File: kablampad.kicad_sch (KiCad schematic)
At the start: 25 parts, among them U1 RP2040_Zero

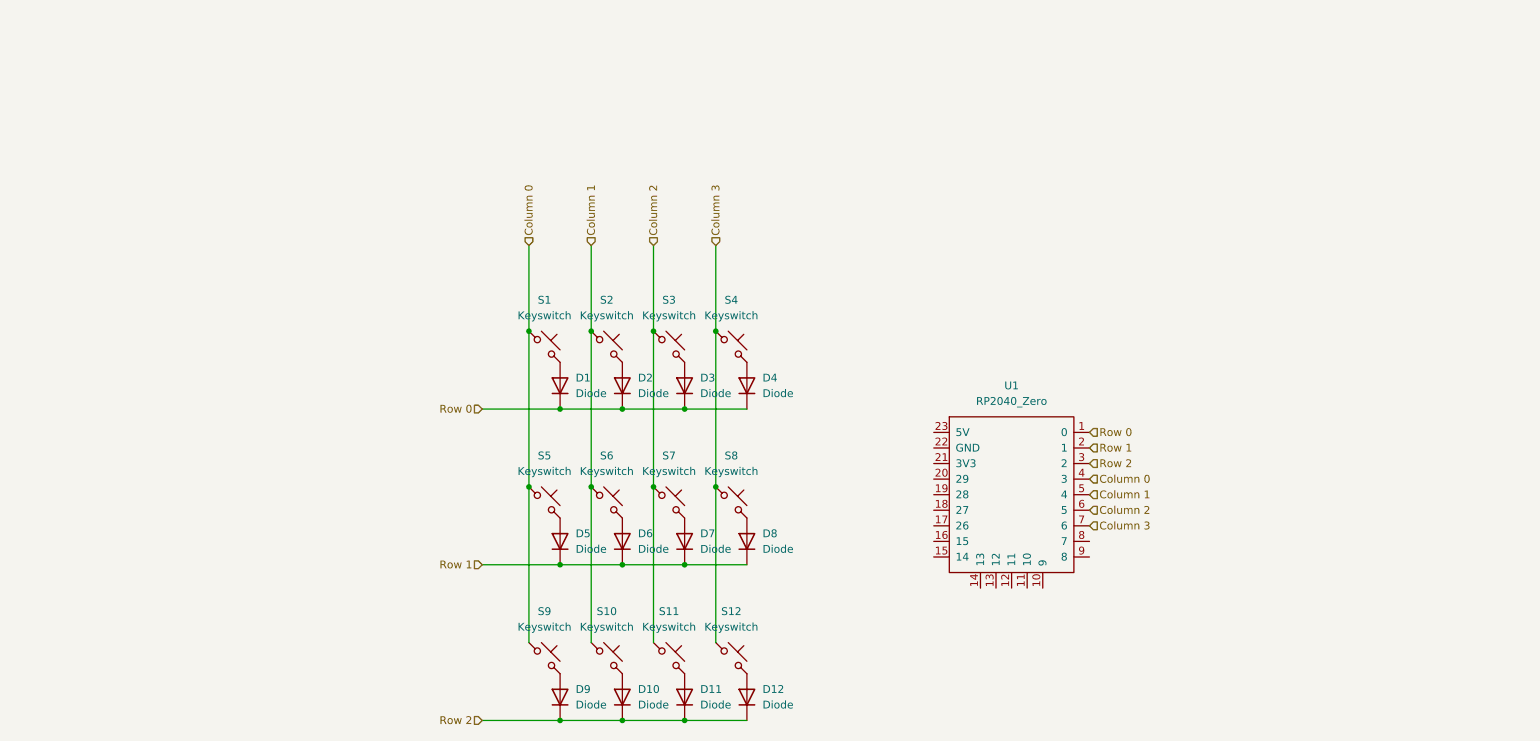
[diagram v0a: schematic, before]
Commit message: made kablamboard v1, idk how i'm gonna merge later (but that's a future problem, yaknow?)
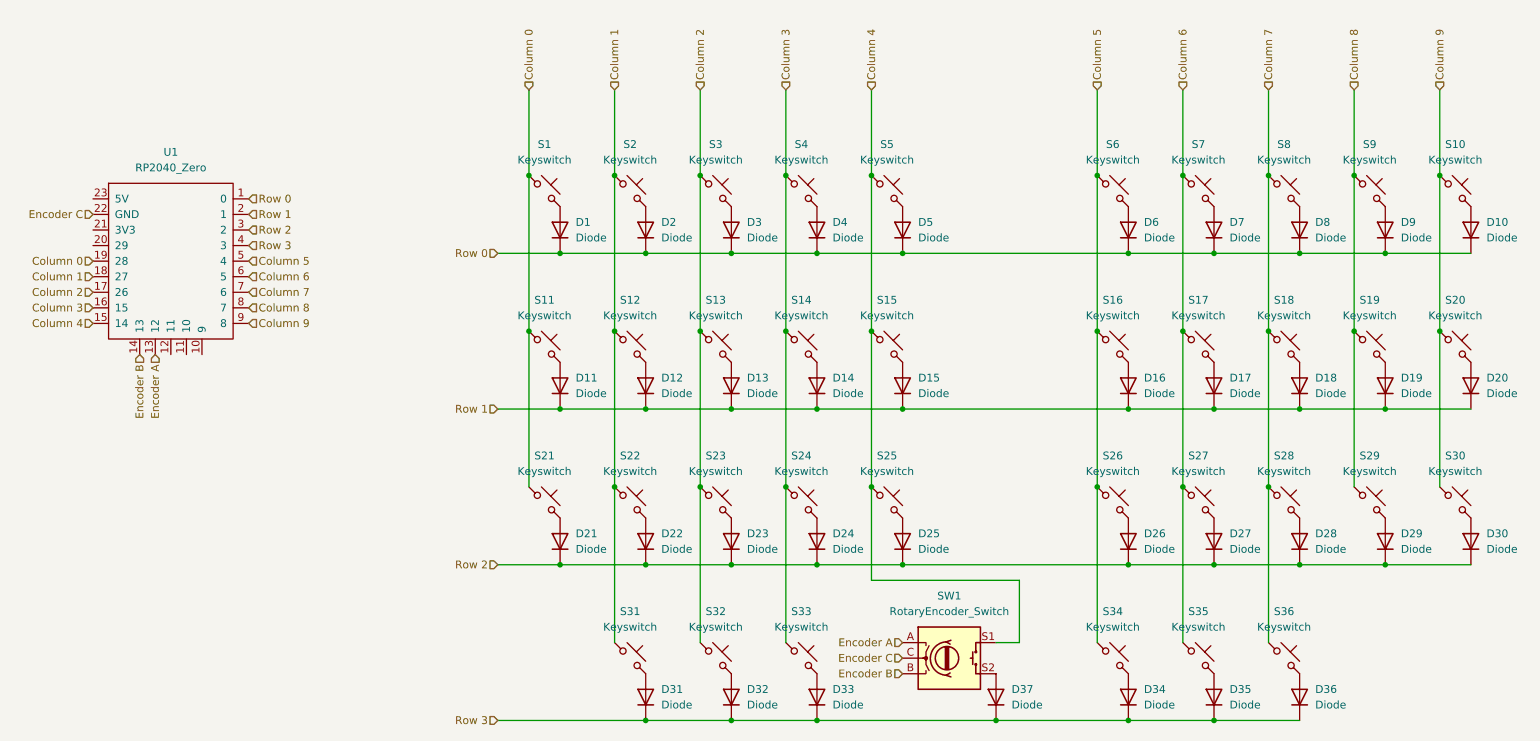
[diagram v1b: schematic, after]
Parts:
- added D13, D14, D15, D16, D17, D18, D19, D20, D21, D22, D23, D24, D25, D26, D27, D28, D29, D30, D31, D32, D33, D34, D35, D36, D37: Diode, ScottoKeebs_Components:Diode_DO-35, symbol ScottoKeebs:Placeholder_Diode
- added S13, S14, S15, S16, S17, S18, S19, S20, S21, S22, S23, S24, S25, S26, S27, S28, S29, S30, S31, S32, S33, S34, S35, S36: Keyswitch, ScottoKeebs_Hotswap:Hotswap_MX_1.00u, symbol ScottoKeebs:Placeholder_Keyswitch
- added SW1: RotaryEncoder_Switch, Rotary_Encoder:RotaryEncoder_Alps_EC11E-Switch_Vertical_H20mm, symbol Device:RotaryEncoder_Switch
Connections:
- net Column 0: now also S11.1, U1.19 (28), S21.1; no longer S5.1, S9.1, U1.4 (3)
- net Column 1: now also S12.1, U1.18 (27), S22.1, S31.1; no longer S10.1, S6.1, U1.5 (4)
- net Column 2: now also U1.17 (26), S13.1, S23.1, S32.1; no longer S11.1, S7.1, U1.6 (5)
- net Column 3: now also U1.16 (15), S14.1, S24.1, S33.1; no longer S12.1, S8.1, U1.7 (6)
- net Row 0: now also D10.1 (K), D5.1 (K), D6.1 (K), D7.1 (K), D8.1 (K), D9.1 (K)
- net Row 1: now also D11.1 (K), D12.1 (K), D13.1 (K), D14.1 (K), D15.1 (K), D16.1 (K), D17.1 (K), D18.1 (K), D19.1 (K), D20.1 (K); no longer D5.1 (K), D6.1 (K), D7.1 (K), D8.1 (K)
- net Row 2: now also D21.1 (K), D22.1 (K), D23.1 (K), D24.1 (K), D25.1 (K), D26.1 (K), D27.1 (K), D28.1 (K), D29.1 (K), D30.1 (K); no longer D10.1 (K), D11.1 (K), D12.1 (K), D9.1 (K)
- net Encoder A: now reaches U1.13 (12)
- net Encoder A: now also SW1.A
- net Encoder B: now reaches U1.14 (13)
- net Encoder B: now also SW1.B
- net Column 4: now reaches U1.15 (14)
- net Column 4: now also S5.1, S15.1, S25.1, SW1.S1
- net Encoder C: now reaches U1.22 (GND)
- net Encoder C: now also SW1.C
- net Column 8: now reaches U1.8 (7)
- net Column 8: now also S9.1, S19.1, S29.1
- net Column 9: now reaches U1.9 (8)
- net Column 9: now also S10.1, S20.1, S30.1
- new net: D35.2 (A), S35.2
- new net: D20.2 (A), S20.2
- new net: D31.2 (A), S31.2
- new net: D29.2 (A), S29.2
- new net: D27.2 (A), S27.2
- new net: D14.2 (A), S14.2
- new net: D28.2 (A), S28.2
- new net: D33.2 (A), S33.2
- new net: D15.2 (A), S15.2
- new net: D30.2 (A), S30.2
- new net: D23.2 (A), S23.2
- new net: D17.2 (A), S17.2
- new net: D19.2 (A), S19.2
- new net: D26.2 (A), S26.2
- new net: D34.2 (A), S34.2
- new net: D24.2 (A), S24.2
- new net: D16.2 (A), S16.2
- new net: D37.2 (A), SW1.S2
- new net: D13.2 (A), S13.2
- new net: D32.2 (A), S32.2
- new net: D22.2 (A), S22.2
- new net: D21.2 (A), S21.2
- new net: D18.2 (A), S18.2
- new net: D36.2 (A), S36.2
- new net: D25.2 (A), S25.2
- new net Column 5: S16.1, S26.1, S34.1, S6.1, U1.5 (4)
- new net Column 6: S17.1, S27.1, S35.1, S7.1, U1.6 (5)
- new net Column 7: S18.1, S28.1, S36.1, S8.1, U1.7 (6)
- new net Row 3: D31.1 (K), D32.1 (K), D33.1 (K), D34.1 (K), D35.1 (K), D36.1 (K), D37.1 (K), U1.4 (3)
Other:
- moved on the sheet: D1, D2, D3, S1, S2, S3, U1
